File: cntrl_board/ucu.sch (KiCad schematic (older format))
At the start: 127 parts, among them J2 AMP_1, J24 AMP_4, J25 AMP_5, J26 AMP_6, J3 BUTTON, J4 AMP_2, J40 LCD, J41 TempSens1, J42 TempSens2, J47 USB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

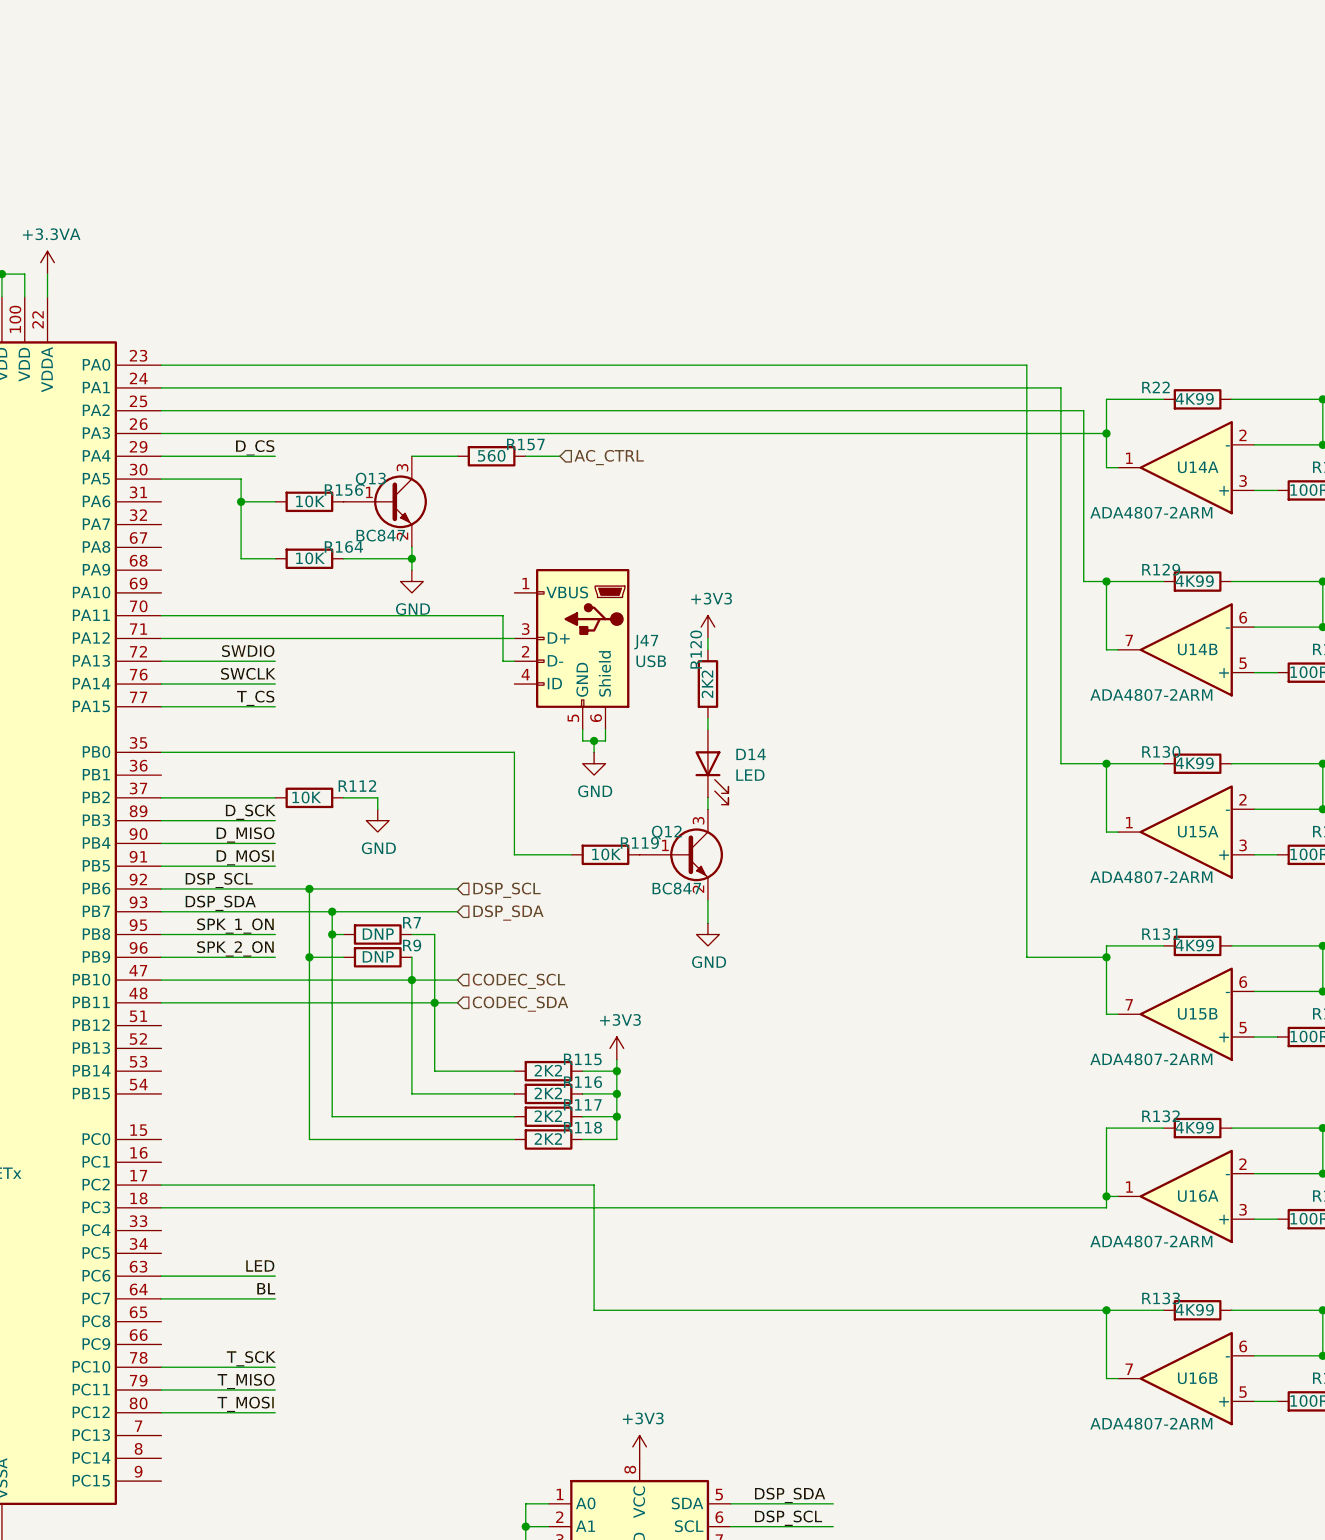
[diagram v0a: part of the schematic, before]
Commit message: update xformer soft startup
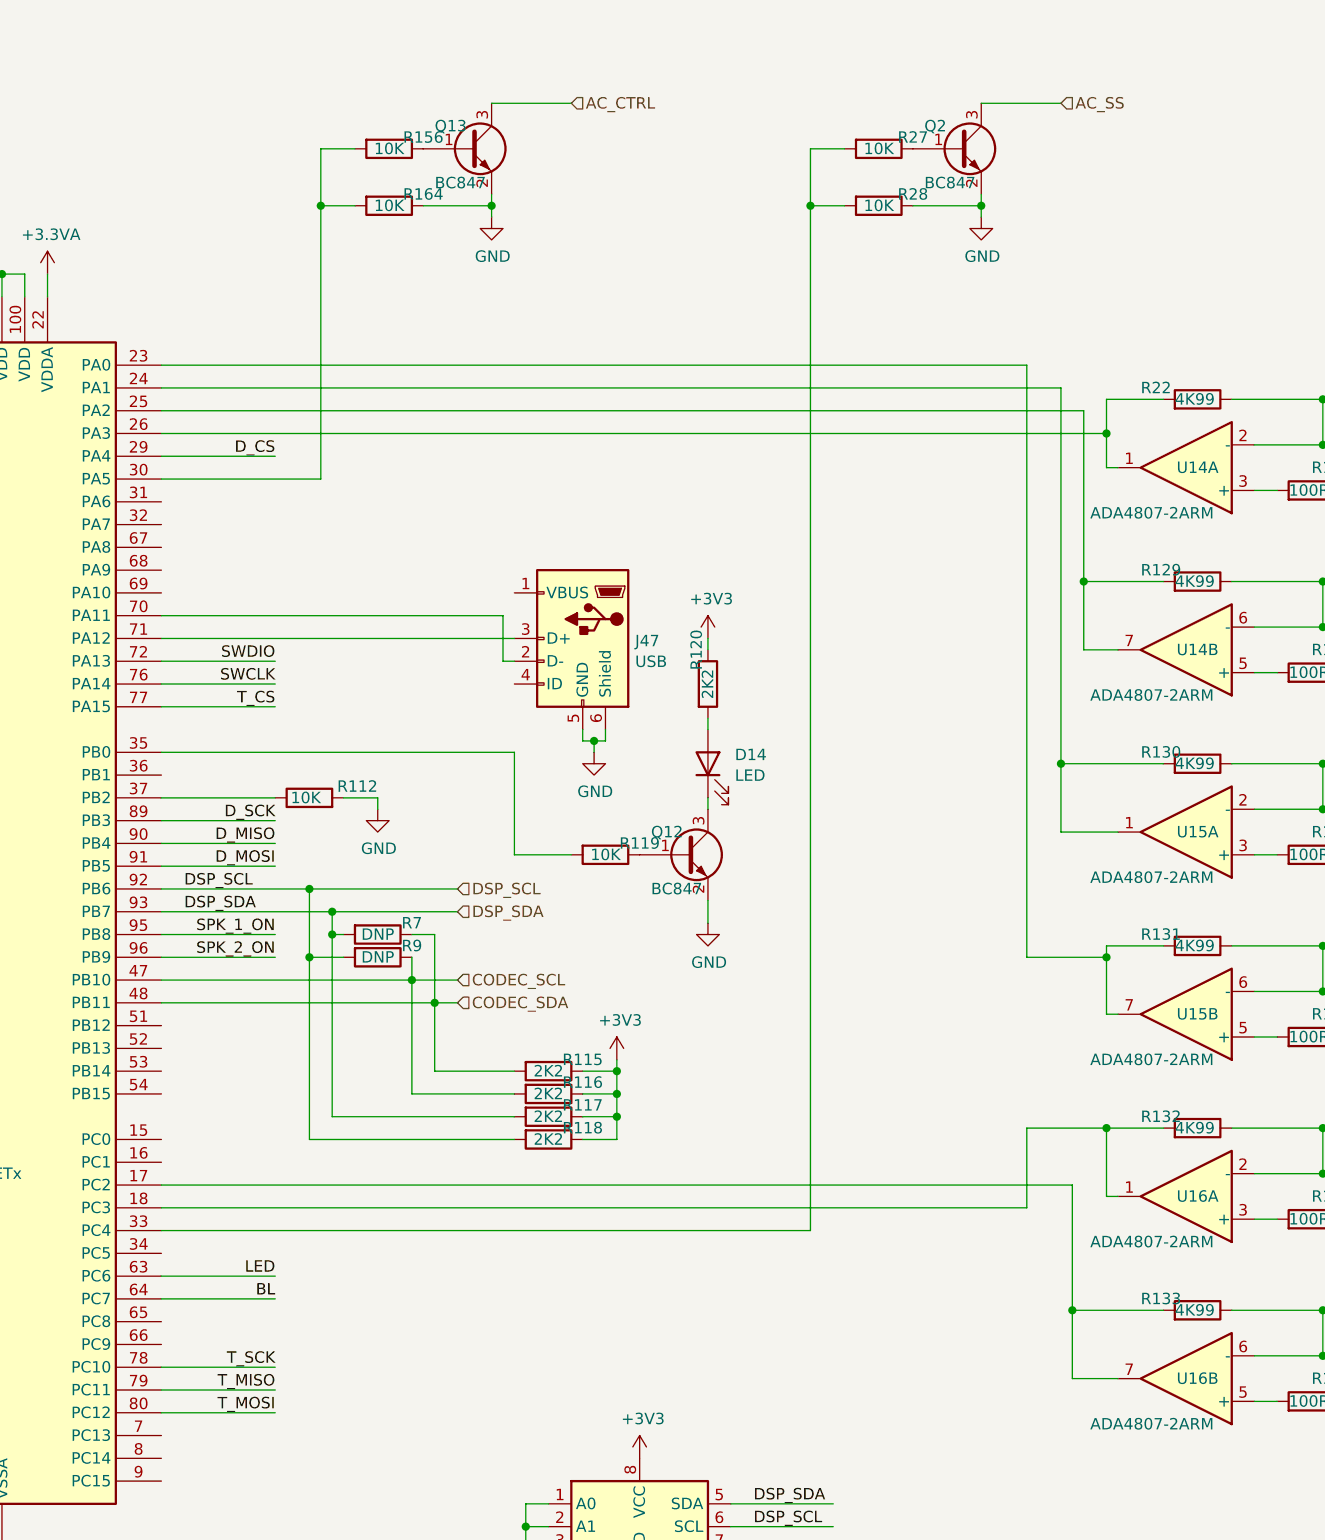
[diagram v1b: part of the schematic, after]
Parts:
- removed R157: 560, Resistor_SMD:R_0603_1608Metric_Pad0.98x0.95mm_HandSolder, symbol Device:R
- added Q2: BC847, Package_TO_SOT_SMD:SOT-23, symbol Device:Q_NPN_BEC
- added R27, R28: 10K, Resistor_SMD:R_0603_1608Metric_Pad0.98x0.95mm_HandSolder, symbol Device:R
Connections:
- net AC_CTRL: now also Q13.3 (C)
- net GND: now also Q2.2 (E), R28.1
- net at U4.33 (PC4): now also R27.2, R28.2
- new net: Q2.1 (B), R27.1
- new net AC_SS: Q2.3 (C)
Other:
- moved on the sheet: Q13, R156, R164
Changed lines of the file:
@@
 Wire Wire Line
 	2750 5350 2150 5350
-Text HLabel 6300 3350 2    50   Input ~ 0
-AC_CTRL
 $Comp
 L Device:R R9
@@
 	9750 7500 9950 7500
 Wire Wire Line
-	8750 7400 8700 7400
-Wire Wire Line
-	8700 7400 8700 7100
-Wire Wire Line
-	8700 7100 8950 7100
+	8550 7400 8550 7100
 Wire Wire Line
 	8750 6600 8700 6600
@@
 Wire Wire Line
 	8700 5500 8950 5500
-Wire Wire Line
-	8750 5000 8700 5000
-Wire Wire Line
-	8700 5000 8700 4700
-Wire Wire Line
-	8700 4700 8950 4700
-Wire Wire Line
-	8750 4200 8700 4200
-Wire Wire Line
-	8700 4200 8700 3900
-Wire Wire Line
-	8700 3900 8950 3900
 Wire Wire Line
 	8750 3400 8700 3400
@@
 L Device:Q_NPN_BEC Q13
 U 1 1 6339A27A
-P 5550 3550
-F 0 "Q13" H 5400 3650 50  0000 L CNN
-F 1 "BC847" H 5400 3400 50  0000 L CNN
-F 2 "Package_TO_SOT_SMD:SOT-23" H 5750 3650 50  0001 C CNN
-F 3 "~" H 5550 3550 50  0001 C CNN
-	1    5550 3550
+P 5900 2000
+F 0 "Q13" H 5750 2100 50  0000 L CNN
+F 1 "BC847" H 5750 1850 50  0000 L CNN
+F 2 "Package_TO_SOT_SMD:SOT-23" H 6100 2100 50  0001 C CNN
+F 3 "~" H 5900 2000 50  0001 C CNN
+	1    5900 2000
 	1    0    0    -1
 $EndComp
@@
 L Device:R R156
 U 1 1 6339A280
-P 5200 3550
-F 0 "R156" V 5150 3700 50  0000 C CNN
-F 1 "10K" V 5200 3550 50  0000 C CNN
-F 2 "Resistor_SMD:R_0603_1608Metric_Pad0.98x0.95mm_HandSolder" V 5130 3550 50  0001 C CNN
-F 3 "~" H 5200 3550 50  0001 C CNN
-	1    5200 3550
+P 5550 2000
+F 0 "R156" V 5500 2150 50  0000 C CNN
+F 1 "10K" V 5550 2000 50  0000 C CNN
+F 2 "Resistor_SMD:R_0603_1608Metric_Pad0.98x0.95mm_HandSolder" V 5480 2000 50  0001 C CNN
+F 3 "~" H 5550 2000 50  0001 C CNN
+	1    5550 2000
 	0    1    1    0
 $EndComp
@@
 L power:GND #PWR0185
 U 1 1 6339A286
-P 5650 3850
-F 0 "#PWR0185" H 5650 3600 50  0001 C CNN
-F 1 "GND" H 5655 3677 50  0000 C CNN
-F 2 "" H 5650 3850 50  0001 C CNN
-F 3 "" H 5650 3850 50  0001 C CNN
-	1    5650 3850
-	1    0    0    -1
-$EndComp
-Wire Wire Line
-	5650 3750 5650 3800
-Wire Wire Line
-	5050 3550 4900 3550
-Wire Wire Line
-	4900 3550 4900 3450
-Wire Wire Line
-	4900 3450 4550 3450
-$Comp
-L Device:R R157
-U 1 1 634C1204
-P 6000 3350
-F 0 "R157" V 5950 3500 50  0000 C CNN
-F 1 "560" V 6000 3350 50  0000 C CNN
-F 2 "Resistor_SMD:R_0603_1608Metric_Pad0.98x0.95mm_HandSolder" V 5930 3350 50  0001 C CNN
-F 3 "~" H 6000 3350 50  0001 C CNN
-	1    6000 3350
-	0    1    1    0
-$EndComp
-Wire Wire Line
-	5650 3350 5850 3350
-Wire Wire Line
-	6150 3350 6300 3350
+P 6000 2300
+F 0 "#PWR0185" H 6000 2050 50  0001 C CNN
+F 1 "GND" H 6005 2127 50  0000 C CNN
+F 2 "" H 6000 2300 50  0001 C CNN
+F 3 "" H 6000 2300 50  0001 C CNN
+	1    6000 2300
+	1    0    0    -1
+$EndComp
+Wire Wire Line
+	6000 2200 6000 2250
+Wire Wire Line
+	5400 2000 5250 2000
 Text HLabel 11200 4100 2    50   Input ~ 0
 AMP_REF_IN
@@
 	8600 3150 8600 3900
 Wire Wire Line
-	8600 3900 8700 3900
-Connection ~ 8700 3900
-Wire Wire Line
 	4550 3050 8500 3050
 Wire Wire Line
 	8500 3050 8500 4700
-Wire Wire Line
-	8500 4700 8700 4700
-Connection ~ 8700 4700
 Wire Wire Line
 	4550 2950 8350 2950
@@
 	8700 5550 8700 5500
 Wire Wire Line
-	4550 6550 6450 6550
-Wire Wire Line
-	6450 6550 6450 7100
-Wire Wire Line
-	6450 7100 8700 7100
-Connection ~ 8700 7100
-Wire Wire Line
-	4550 6650 8700 6650
-Wire Wire Line
-	8700 6650 8700 6600
-Connection ~ 8700 6600
+	4550 6650 8350 6650
 $Comp
 L Device:R R164
 U 1 1 610D3039
-P 5200 3800
-F 0 "R164" V 5150 3950 50  0000 C CNN
-F 1 "10K" V 5200 3800 50  0000 C CNN
-F 2 "Resistor_SMD:R_0603_1608Metric_Pad0.98x0.95mm_HandSolder" V 5130 3800 50  0001 C CNN
-F 3 "~" H 5200 3800 50  0001 C CNN
-	1    5200 3800
+P 5550 2250
+F 0 "R164" V 5500 2400 50  0000 C CNN
+F 1 "10K" V 5550 2250 50  0000 C CNN
+F 2 "Resistor_SMD:R_0603_1608Metric_Pad0.98x0.95mm_HandSolder" V 5480 2250 50  0001 C CNN
+F 3 "~" H 5550 2250 50  0001 C CNN
+	1    5550 2250
 	0    1    1    0
 $EndComp
 Wire Wire Line
-	4900 3550 4900 3800
-Wire Wire Line
-	4900 3800 5050 3800
-Connection ~ 4900 3550
-Wire Wire Line
-	5350 3800 5650 3800
-Connection ~ 5650 3800
-Wire Wire Line
-	5650 3800 5650 3850
+	5250 2000 5250 2250
+Wire Wire Line
+	5250 2250 5400 2250
+Wire Wire Line
+	5700 2250 6000 2250
+Connection ~ 6000 2250
+Wire Wire Line
+	6000 2250 6000 2300
 $Comp
 L Memory_EEPROM:24LC64 U21
@@
 Wire Wire Line
 	2250 6650 2750 6650
+Text HLabel 6350 1800 2    50   Input ~ 0
+AC_CTRL
+$Comp
+L Device:Q_NPN_BEC Q2
+U 1 1 61B2ACF9
+P 8050 2000
+F 0 "Q2" H 7900 2100 50  0000 L CNN
+F 1 "BC847" H 7900 1850 50  0000 L CNN
+F 2 "Package_TO_SOT_SMD:SOT-23" H 8250 2100 50  0001 C CNN
+F 3 "~" H 8050 2000 50  0001 C CNN
+	1    8050 2000
+	1    0    0    -1
+$EndComp
+$Comp
+L Device:R R27
+U 1 1 61B2ACFF
+P 7700 2000
+F 0 "R27" V 7650 2150 50  0000 C CNN
+F 1 "10K" V 7700 2000 50  0000 C CNN
+F 2 "Resistor_SMD:R_0603_1608Metric_Pad0.98x0.95mm_HandSolder" V 7630 2000 50  0001 C CNN
+F 3 "~" H 7700 2000 50  0001 C CNN
+	1    7700 2000
+	0    1    1    0
+$EndComp
+$Comp
+L power:GND #PWR0204
+U 1 1 61B2AD05
+P 8150 2300
+F 0 "#PWR0204" H 8150 2050 50  0001 C CNN
+F 1 "GND" H 8155 2127 50  0000 C CNN
+F 2 "" H 8150 2300 50  0001 C CNN
+F 3 "" H 8150 2300 50  0001 C CNN
+	1    8150 2300
+	1    0    0    -1
+$EndComp
+Wire Wire Line
+	8150 2200 8150 2250
+Wire Wire Line
+	7550 2000 7400 2000
+$Comp
+L Device:R R28
+U 1 1 61B2AD16
+P 7700 2250
+F 0 "R28" V 7650 2400 50  0000 C CNN
+F 1 "10K" V 7700 2250 50  0000 C CNN
+F 2 "Resistor_SMD:R_0603_1608Metric_Pad0.98x0.95mm_HandSolder" V 7630 2250 50  0001 C CNN
+F 3 "~" H 7700 2250 50  0001 C CNN
+	1    7700 2250
+	0    1    1    0
+$EndComp
+Wire Wire Line
+	7400 2000 7400 2250
+Wire Wire Line
+	7400 2250 7550 2250
+Wire Wire Line
+	7850 2250 8150 2250
+Connection ~ 8150 2250
+Wire Wire Line
+	8150 2250 8150 2300
+Text HLabel 8500 1800 2    50   Input ~ 0
+AC_SS
+Wire Wire Line
+	5250 3450 5250 2250
+Wire Wire Line
+	4550 3450 5250 3450
+Connection ~ 5250 2250
+Wire Wire Line
+	4550 6750 7400 6750
+Wire Wire Line
+	7400 6750 7400 2250
+Connection ~ 7400 2250
+Wire Wire Line
+	8700 6300 8350 6300
+Wire Wire Line
+	8350 6300 8350 6650
+Connection ~ 8700 6300
+Wire Wire Line
+	8550 7100 8550 6550
+Wire Wire Line
+	4550 6550 8550 6550
+Connection ~ 8550 7100
+Wire Wire Line
+	8550 7100 8950 7100
+Wire Wire Line
+	8550 7400 8750 7400
+Wire Wire Line
+	8500 5000 8500 4700
+Connection ~ 8500 4700
+Wire Wire Line
+	8500 5000 8750 5000
+Wire Wire Line
+	8500 4700 8950 4700
+Wire Wire Line
+	8600 3900 8950 3900
+Wire Wire Line
+	8600 3900 8600 4200
+Wire Wire Line
+	8600 4200 8750 4200
+Connection ~ 8600 3900
+Wire Wire Line
+	6000 1800 6350 1800
+Wire Wire Line
+	8150 1800 8500 1800
 $EndSCHEMATC
